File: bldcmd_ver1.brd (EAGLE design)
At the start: 43 x 49 mm, 94 parts, among them IC1 STSPIN32F0, IC2 AS5047P-ATSM, IC3 ADM4852ACPZ-REEL7, J1 DF65-3P-1.7V(21), Q1 PSMN2R4-30MLD, Q2 PSMN2R4-30MLD, Q3 PSMN2R4-30MLD, Q4 PSMN2R4-30MLD, Q5 PSMN2R4-30MLD, Q6 PSMN2R4-30MLD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

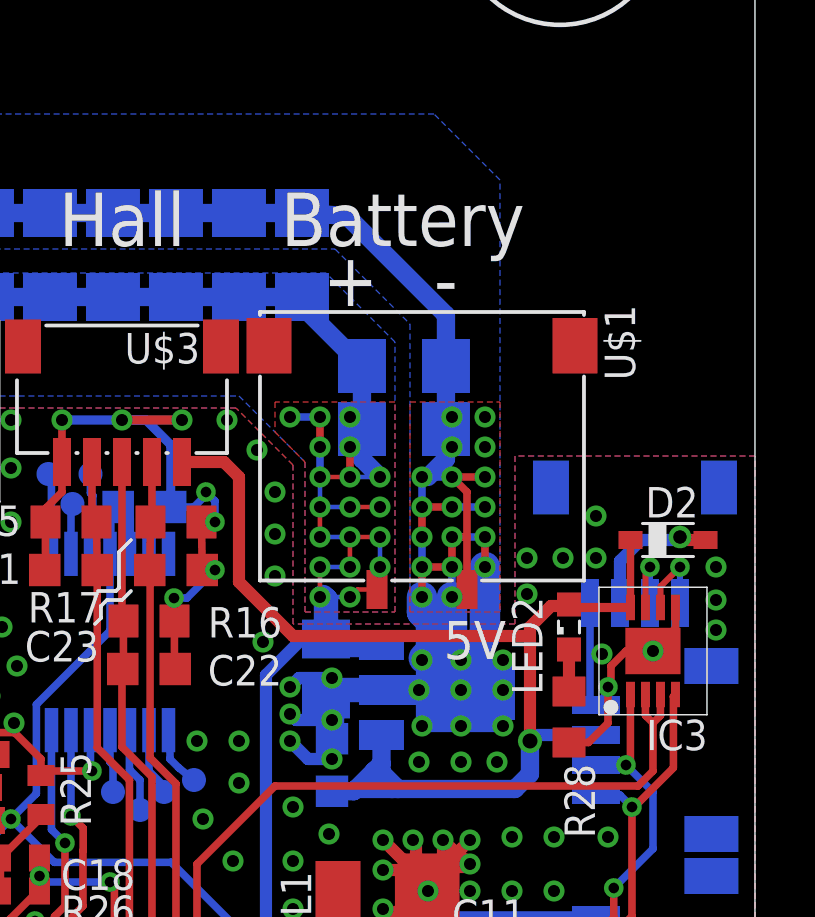
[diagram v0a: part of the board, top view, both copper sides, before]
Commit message: 電源コネクタをES9からDF61に変更
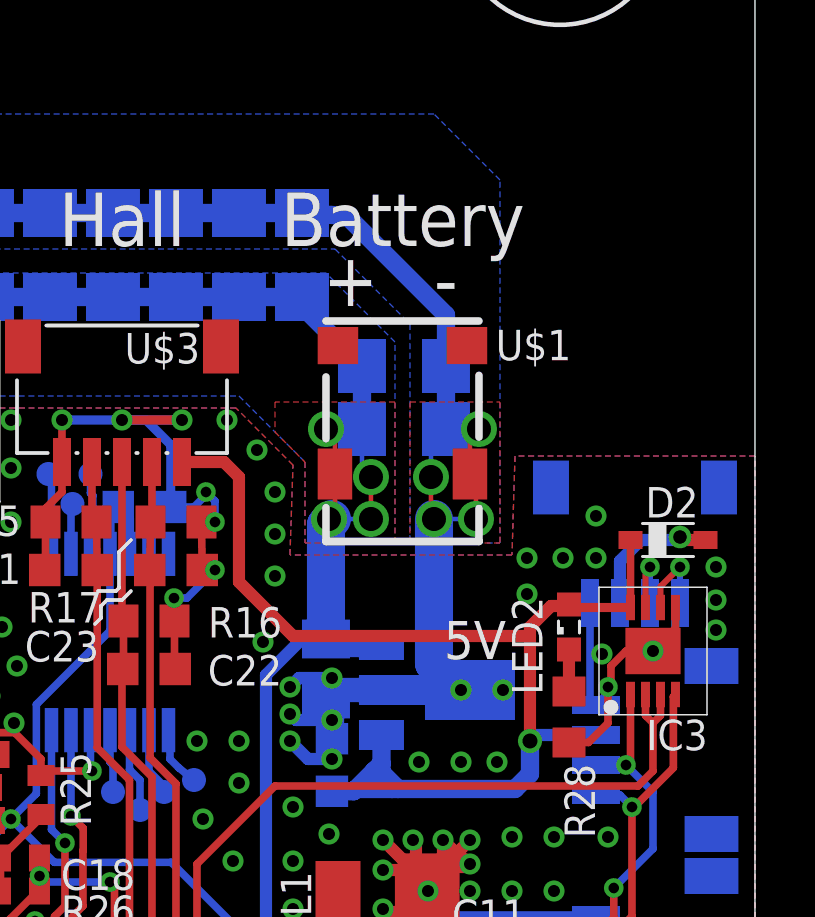
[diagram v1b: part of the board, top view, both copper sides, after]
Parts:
- U$1: value ES9P002VFZ -> DF61-2P-2.2V(23); device rcssl_lib:ES9P002VFZ -> SamacSys_Parts:DF61-2P-2.2V
- moved U$1 9.79 mm to (33.8, 32.7)
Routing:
- net GND: track 332.7 -> 308.3 mm, vias 177 -> 156
- net +12V: track 92.2 -> 82.2 mm, vias 22 -> 7

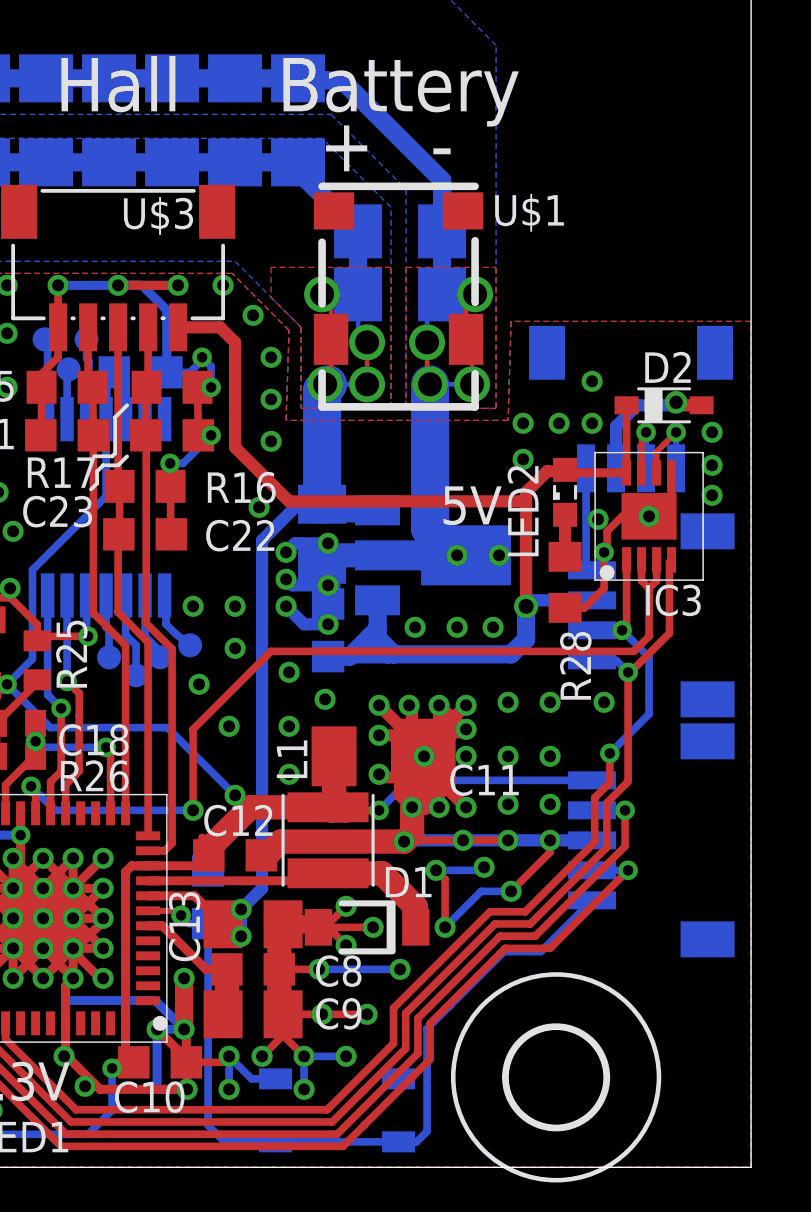
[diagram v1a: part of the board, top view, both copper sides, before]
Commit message: DF61-2P-2.2V(23) の修正を適用
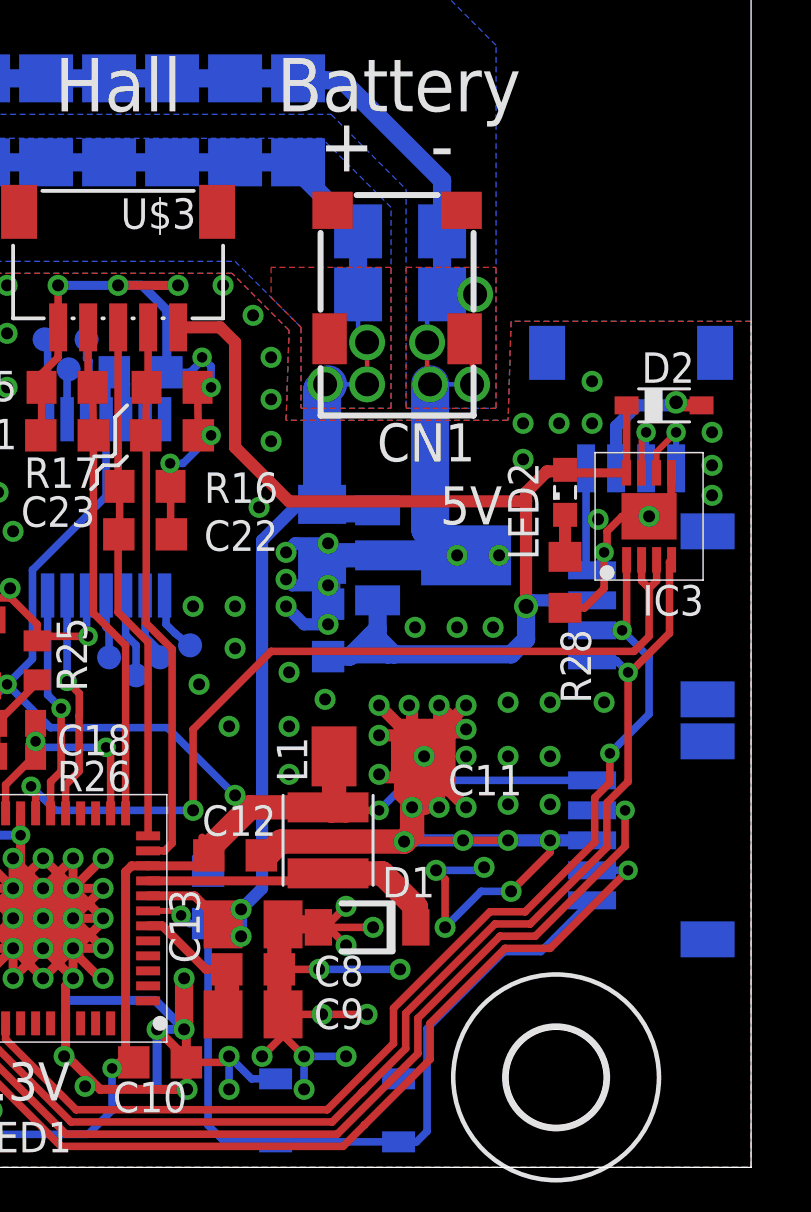
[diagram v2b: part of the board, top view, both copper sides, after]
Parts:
- removed U$1: DF61-2P-2.2V(23), SamacSys_Parts:DF61-2P-2.2V
- added CN1: DF61-2P-2.2V(23), SamacSys_Parts:DF61-2P-2.2V
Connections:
- net +12V: now also CN1.2; no longer U$1.2
- net GND: now also CN1.1; no longer U$1.1
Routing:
- net +12V: track 82.2 -> 79.3 mm, vias 7 -> 6
- net GND: track 308.3 -> 306.8 mm

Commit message: DF65のライブラリ場所の変更を適用
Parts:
- CN1: device SamacSys_Parts:DF61-2P-2.2V -> scramble-con-hirose:DF61-2P-2.2V
- J1: device rcssl_lib:DF65-3P-1.7V(21) -> scramble-con-hirose:DF65-3P-1.7V
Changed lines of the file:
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@@
 <text x="19.8" y="35.2" size="1.778" layer="21">Hall</text>
 <text x="11" y="35.2" size="1.778" layer="21">Motor</text>
-<text x="28.6" y="33.2" size="1.778" layer="21" ratio="12">+</text>
-<text x="32.3" y="33.2" size="1.778" layer="21" ratio="12">-</text>
+<text x="29.7" y="32.7" size="1.778" layer="21" ratio="12">+</text>
+<text x="31.7" y="32.7" size="1.778" layer="21" ratio="12">-</text>
 <wire x1="21.1" y1="23.7" x2="21.7" y2="23.7" width="0.127" layer="21"/>
 <wire x1="21.7" y1="23.7" x2="21.8" y2="23.8" width="0.127" layer="21"/>
@@
 <attribute name="VALUE" x="29" y="11.6" size="1.016" layer="27"/>
 </element>
-<element name="J1" library="rcssl_lib" package="DF65-3P-1.7V(21)" value="DF65-3P-1.7V(21)" x="14" y="29.7" smashed="yes" rot="R180">
+<element name="J1" library="scramble-con-hirose" package="DF65-3P-1.7V" value="DF65-3P-1.7V(21)" x="14" y="29.7" smashed="yes" rot="R180">
 <attribute name="3D_PACKAGE" value="" x="14" y="29.7" size="1.778" layer="27" rot="R180" display="off"/>
 <attribute name="ALLIED_NUMBER" value="" x="14" y="29.7" size="1.778" layer="27" rot="R180" display="off"/>
@@
 <element name="H7" library="holes" library_urn="urn:adsk.eagle:library:237" package="3,2" package3d_urn="urn:adsk.eagle:package:14275/1" value="MOUNT-HOLE3.2" x="36.5" y="46" locked="yes"/>
 <element name="H8" library="holes" library_urn="urn:adsk.eagle:library:237" package="3,2" package3d_urn="urn:adsk.eagle:package:14275/1" value="MOUNT-HOLE3.2" x="6.5" y="46" locked="yes"/>
-<element name="CN1" library="SamacSys_Parts" package="DF61-2P-2.2V" value="DF61-2P-2.2V(23)" x="31.2" y="29.3" rot="R180">
+<element name="CN1" library="scramble-con-hirose" package="DF61-2P-2.2V" value="DF61-2P-2.2V(23)" x="31.2" y="29.3" smashed="yes" rot="R180">
 <attribute name="3D_PACKAGE" value="" x="31.2" y="29.3" size="1.778" layer="27" rot="R180" display="off"/>
 <attribute name="ALLIED_NUMBER" value="" x="31.2" y="29.3" size="1.778" layer="27" rot="R180" display="off"/>
@@
 <attribute name="MANUFACTURER_NAME" value="Hirose" x="31.2" y="29.3" size="1.778" layer="27" rot="R180" display="off"/>
 <attribute name="MANUFACTURER_PART_NUMBER" value="DF61-2P-2.2V(23)" x="31.2" y="29.3" size="1.778" layer="27" rot="R180" display="off"/>
+<attribute name="NAME" x="35.4" y="30.2" size="1.27" layer="25" ratio="12" rot="R90"/>
 <attribute name="OTHER_PART_NUMBER" value="" x="31.2" y="29.3" size="1.778" layer="27" rot="R180" display="off"/>
 <attribute name="RS_PART_NUMBER" value="7922837P" x="31.2" y="29.3" size="1.778" layer="27" rot="R180" display="off"/>
 <attribute name="SUPPLIER_NAME" value="RS" x="31.2" y="29.3" size="1.778" layer="27" rot="R180" display="off"/>
+<attribute name="VALUE" x="33.8" y="33.9" size="1.27" layer="27" font="vector" ratio="12" rot="R180"/>
 </element>
 </elements>
